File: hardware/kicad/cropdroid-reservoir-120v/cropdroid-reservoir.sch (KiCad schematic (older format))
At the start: 23 parts, among them CON1 SJ1-3523N, CON2 SJ1-3523N, CON3 SJ1-3523N, CON4 SJ1-3523N, CON5 SJ1-3523N, CON6 SJ1-3523N, CON7 SJ1-3523N, J1 OSTTC020162, J2 640456-3, J3 OSTTC020162, J4 OSTTC020162, J5 SAMTEC-MTSW-118-10-X-D-640, J6 PJ-102A, K1 T9AS1D12-15, K2 T9AS1D12-15, K3 T9AS1D12-15, Q1 ULN2003AN

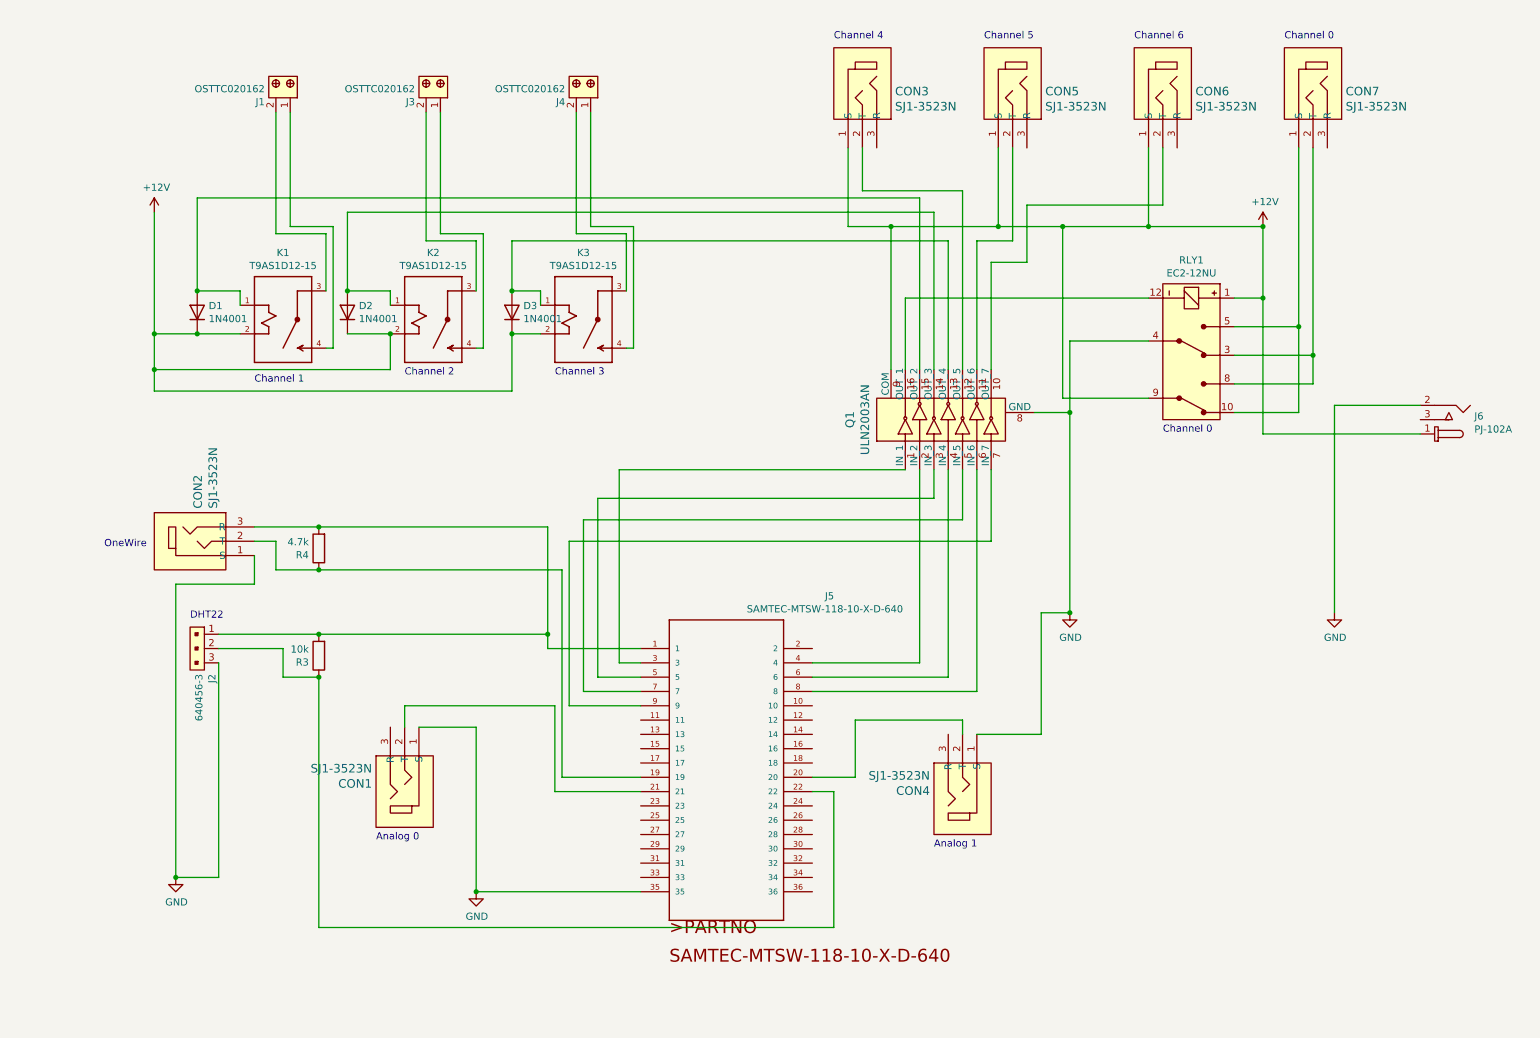
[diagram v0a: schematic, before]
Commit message: add cropdroid-reservoir-120v design
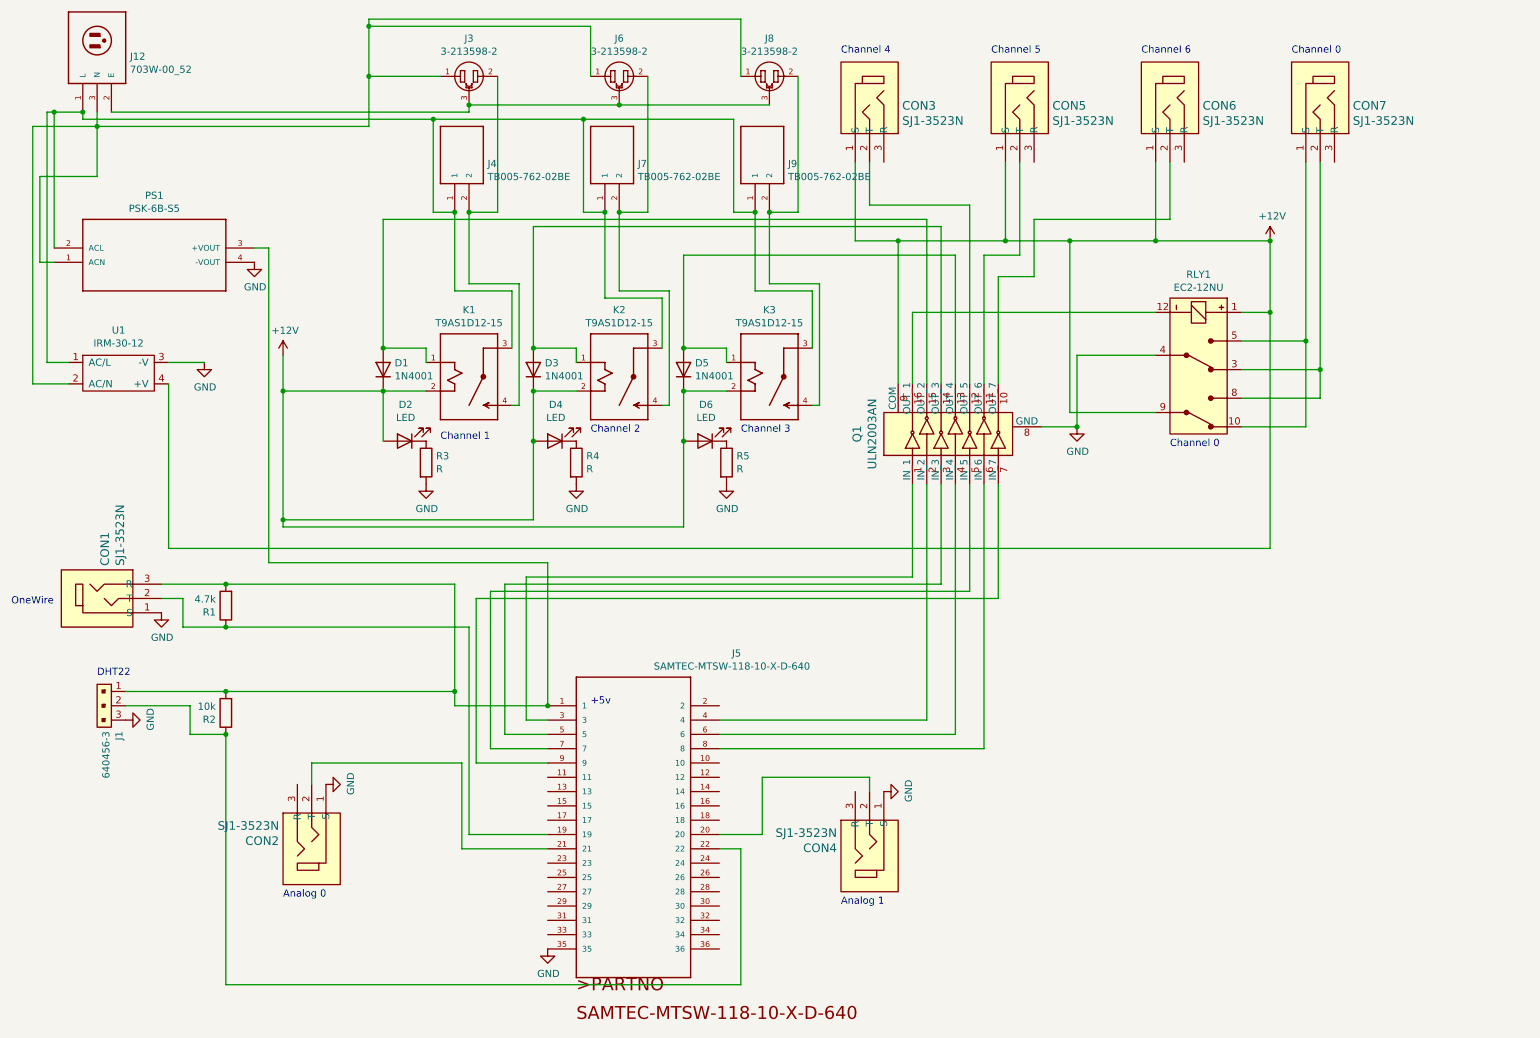
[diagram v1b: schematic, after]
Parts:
- removed J1, J3, J4: OSTTC020162, digikey-footprints:Term_Block_1x2_P5mm, symbol dk_Terminal-Blocks-Wire-to-Board:OSTTC020162
- removed J6: PJ-102A, digikey-footprints:Barrel_Jack_5.5mmODx2.1mmID_PJ-102A, symbol dk_Barrel-Power-Connectors:PJ-102A
- added D2, D4, D6: LED, libraries:CAPPRD350W60D800H2000, symbol Device:LED
- added J12: 703W-00_52, 703W-00_54:52, symbol 703W-00_52:703W-00_52
- added J3, J6, J8: 3-213598-2, 3-213598-2:TE_3-213598-2, symbol 3-213598-2:3-213598-2
- added J4, J7, J9: TB005-762-02BE, TB005-762-02BE:CUI_TB005-762-02BE, symbol TB005-762-02BE:TB005-762-02BE
- added PS1: PSK-6B-S5, PSK-6B-S5:CONV_PSK-6B-S5, symbol PSK-6B-S5:PSK-6B-S5
- added R3, R4, R5: R, Resistor_THT:R_Axial_DIN0207_L6.3mm_D2.5mm_P10.16mm_Horizontal, symbol Device:R
- added U1: IRM-30-12, IRM-30-12:IRM-30-12, symbol IRM-30-12:IRM-30-12
- renumbered CON2 to CON1, CON1 to CON2, D2 to D3, D3 to D5, J2 to J1, R4 to R1, R3 to R2
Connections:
- net +12V: now also D2.2 (A), D4.2 (A), D6.2 (A), U1.4 (+V)
- net GND: now also PS1.4 (-VOUT), R3.2, R4.2, R5.2, U1.3 (-V)
- net at CON1.3 (R), J1.1, J5.1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: now also PS1.3 (+VOUT)
- net at K1.3 (C): now also K2.3 (C), K3.3 (C), J12.1 (L), J4.1, J7.1, J9.1, PS1.2 (ACL), U1.1 (AC/L)
- net at K1.4 (NO): now also J3.2, J4.2
- net at K2.4 (NO): now also J6.2, J7.2
- net at K3.4 (NO): now also J8.2, J9.2
- new net: J12.2 (E), J3.3, J6.3, J8.3
- new net: J12.3 (N), J3.1, J6.1, J8.1, PS1.1 (ACN), U1.2 (AC/N)
- new net: D2.1 (K), R3.1
- new net: D4.1 (K), R4.1
- new net: D6.1 (K), R5.1
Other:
- note added: "+5v"
- moved on the sheet: CON1, CON2, CON3, CON4, CON5, CON6, CON7, D1, D3, D5, J1, J5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
